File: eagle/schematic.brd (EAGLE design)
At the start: 40 x 40 mm, 23 parts, among them IC1 PIC18F1320SO, U1 MIC5205, U2 SG-3040LCLC

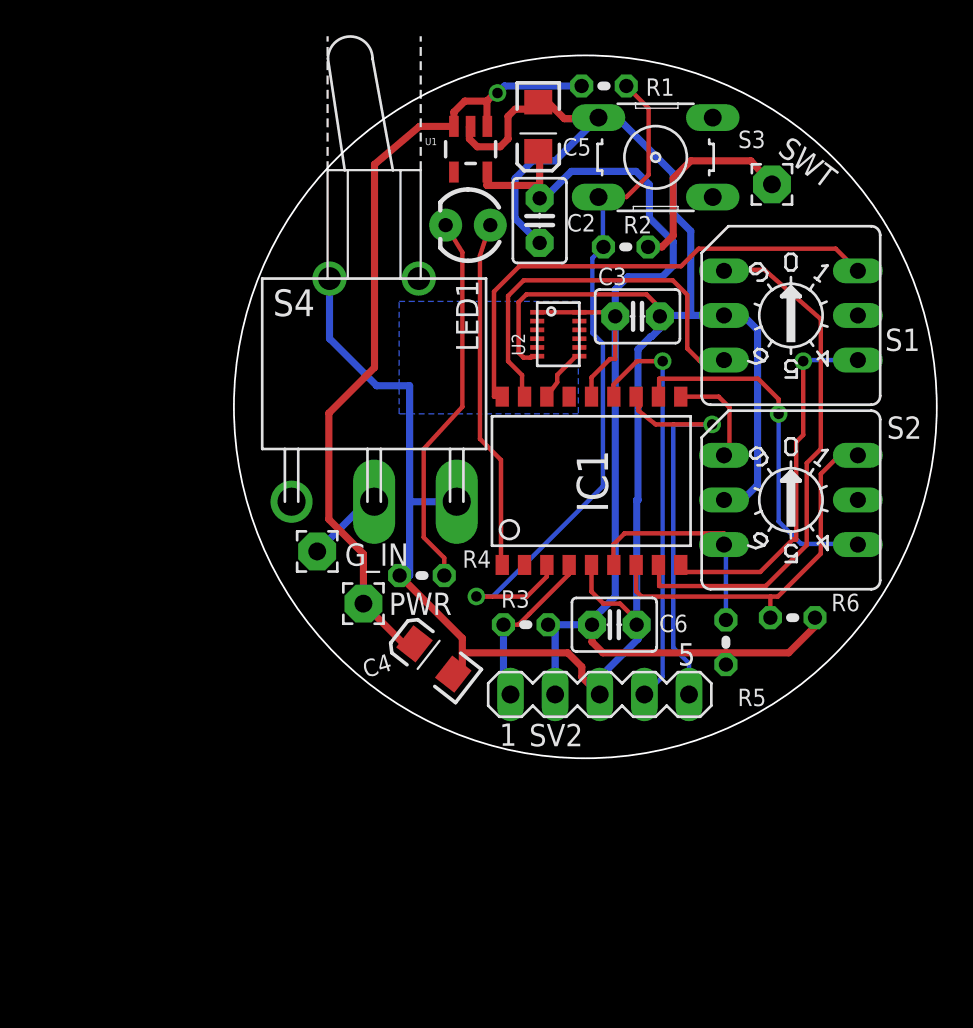
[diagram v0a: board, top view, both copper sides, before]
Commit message: Replaced ICD board header with a JST-EH connector
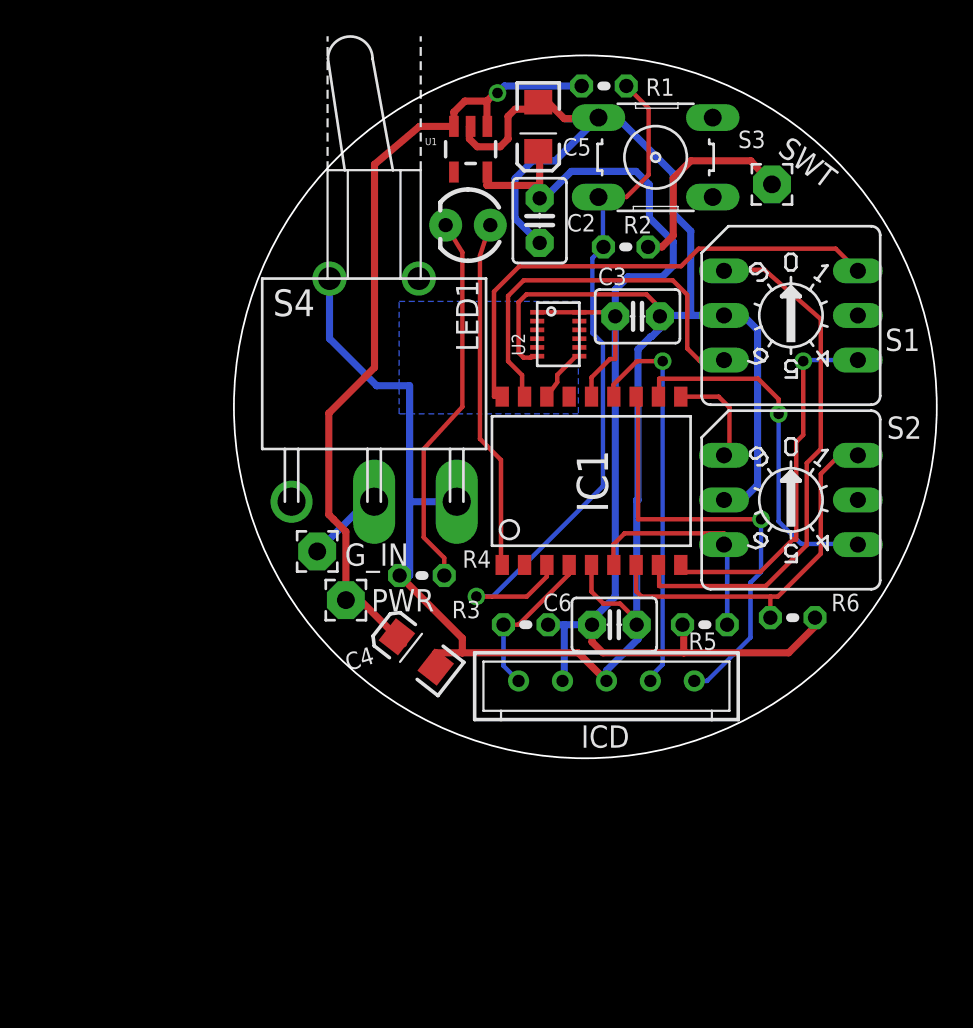
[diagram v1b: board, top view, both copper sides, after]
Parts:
- removed SV2: ICD, con-lstb:MA05-1
- added ICD: B4B-ZR, untitled:B5B-EH
- R5, R6: value 4.7K -> 10K
- moved R5 1.56 mm to (26.8, 7.60), turned to 180 degrees
- moved C4 1.08 mm to (10.4, 6.05)
- moved PWR 1.02 mm to (6.37, 9.00)
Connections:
- net GND: now also ICD.3; no longer SV2.3
- net N$6: now also ICD.1; no longer SV2.1
- net N$7: now also ICD.4; no longer SV2.4
- net N$8: now also ICD.5; no longer SV2.5
- net VDD: now also ICD.2; no longer SV2.2
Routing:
- net N$8: track 23.2 -> 25.3 mm
- net N$7: track 23.5 -> 22.5 mm
- net GND: track 136.8 -> 136.2 mm
- net N$6: track 9.98 -> 9.40 mm

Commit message: Added larger JC variant of oscillator to the underside of the PCB
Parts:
- added U$1: SG-3030,40(LC,JC,JF)JC, untitled:JC_TYPE
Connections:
- net CLK: now also U$1.3
- net GND: now also U$1.2
- net VDD: now also U$1.1, U$1.4
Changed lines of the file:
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@@
 <attribute name="NAME" x="19.75" y="0.6" size="1.27" layer="25"/>
 </element>
+<element name="U$1" library="untitled" package="JC_TYPE" value="SG-3030,40(LC,JC,JF)JC" x="-6" y="-10"/>
 </elements>
 <signals>
@@
 <wire x1="23" y1="6.785584375" x2="21.2" y2="4.985584375" width="0.4064" layer="16"/>
 <wire x1="21.2" y1="4.985584375" x2="21.2" y2="4.4" width="0.4064" layer="16"/>
+<contactref element="U$1" pad="2"/>
+<wire x1="-3.46" y1="-12.3" x2="11.4832125" y2="5.188071875" width="0" layer="19" extent="1-1"/>
 </signal>
 <signal name="CLK">
@@
 <wire x1="18.4" y1="21.81491875" x2="18.4" y2="21.4" width="0.254" layer="1"/>
 <wire x1="18.4" y1="21.4" x2="17.81" y2="20.5779" width="0.254" layer="1"/>
+<contactref element="U$1" pad="3"/>
+<wire x1="-3.46" y1="-7.7" x2="17.6032" y2="20.4622" width="0" layer="19" extent="1-1"/>
 </signal>
 <signal name="V+">
@@
 <wire x1="18.7" y1="4.4" x2="18.8" y2="4.4" width="0.4064" layer="16"/>
 <wire x1="18.8" y1="4.4" x2="18.8" y2="7.6" width="0.4064" layer="16"/>
+<contactref element="U$1" pad="1"/>
+<contactref element="U$1" pad="4"/>
+<wire x1="-8.54" y1="-7.7" x2="18.7" y2="4.4" width="0" layer="19" extent="1-1"/>
+<wire x1="-8.54" y1="-12.3" x2="-8.54" y2="-7.7" width="0" layer="19" extent="1-1"/>
 </signal>
 <signal name="N$1">

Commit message: Redo layout of extra oscillator
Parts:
- removed U$1: SG-3030,40(LC,JC,JF)JC, untitled:JC_TYPE
- added U3: SG-3030JC, untitled:JC_TYPE
- U2: value SG-3040LCLC -> SG-3040LC
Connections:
- net CLK: now also U3.3; no longer U$1.3
- net GND: now also U3.2; no longer U$1.2
- net VDD: now also U3.1, U3.4; no longer U$1.1, U$1.4
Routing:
- net VDD: track 74.9 -> 99.3 mm
- net CLK: track 3.36 -> 12.9 mm, vias 0 -> 1
- net GND: track 136.2 -> 141.7 mm
- removed copper zone on layer 16, net GND
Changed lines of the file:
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@@
 <attribute name="VALUE" x="2.718" y="35.18" size="1.524" layer="27" ratio="10" rot="R270"/>
 </element>
-<element name="U2" library="untitled" package="SOJ-12" value="SG-3040LCLC" x="18.46" y="24.13" smashed="yes" rot="R270">
+<element name="U2" library="untitled" package="SOJ-12" value="SG-3040LC" x="18.46" y="24.13" smashed="yes" rot="R270">
 <attribute name="NAME" x="16.187" y="23.5554" size="0.762" layer="25" font="vector" rot="R270" align="center"/>
 </element>
@@
 <attribute name="NAME" x="19.75" y="0.6" size="1.27" layer="25"/>
 </element>
-<element name="U$1" library="untitled" package="JC_TYPE" value="SG-3030,40(LC,JC,JF)JC" x="-6" y="-10"/>
+<element name="U3" library="untitled" package="JC_TYPE" value="SG-3030JC" x="14" y="22.4" smashed="yes" rot="MR180">
+<attribute name="NAME" x="5.41" y="19.66" size="1.27" layer="26" rot="MR90"/>
+<attribute name="VALUE" x="7.12" y="19.66" size="1.27" layer="28" rot="MR90"/>
+</element>
 </elements>
 <signals>
@@
 <wire x1="28.97538125" y1="25.2" x2="27.89" y2="25.2" width="0.4064" layer="16"/>
 <wire x1="10" y1="10.4" x2="10" y2="14.6" width="0.4064" layer="16"/>
-<wire x1="10" y1="14.6" x2="10" y2="21.2" width="0.4064" layer="16"/>
-<polygon width="0.254" layer="16" orphans="yes">
-<vertex x="9.4" y="26"/>
-<vertex x="19.6" y="26"/>
-<vertex x="19.6" y="19.6"/>
-<vertex x="9.4" y="19.6"/>
-</polygon>
+<wire x1="10" y1="14.6" x2="10" y2="17.478890625" width="0.4064" layer="16"/>
+<wire x1="10" y1="17.478890625" x2="9.278890625" y2="18.2" width="0.4064" layer="16"/>
+<wire x1="9.278890625" y1="18.2" x2="6.416521875" y2="18.2" width="0.4064" layer="16"/>
+<wire x1="6.416521875" y1="18.2" x2="5.44" y2="19.176521875" width="0.4064" layer="16"/>
+<wire x1="5.44" y1="19.176521875" x2="5.44" y2="27.3" width="0.4064" layer="16"/>
 <contactref element="S4" pad="3"/>
 <contactref element="S4" pad="B"/>
 <wire x1="13" y1="6" x2="19.6" y2="6" width="0.4064" layer="1"/>
 <wire x1="19.6" y1="6" x2="21.2" y2="4.4" width="0.4064" layer="1"/>
-<wire x1="10" y1="21.2" x2="8.1220875" y2="21.2" width="0.4064" layer="16"/>
-<wire x1="8.1220875" y1="21.2" x2="5.44" y2="23.8820875" width="0.4064" layer="16"/>
-<wire x1="5.44" y1="23.8820875" x2="5.44" y2="27.3" width="0.4064" layer="16"/>
 <wire x1="10" y1="10.4" x2="9.43" y2="10.4" width="0.4064" layer="16"/>
 <wire x1="12.68" y1="14.6" x2="10" y2="14.6" width="0.4064" layer="16"/>
@@
 <wire x1="23" y1="6.785584375" x2="21.2" y2="4.985584375" width="0.4064" layer="16"/>
 <wire x1="21.2" y1="4.985584375" x2="21.2" y2="4.4" width="0.4064" layer="16"/>
-<contactref element="U$1" pad="2"/>
-<wire x1="-3.46" y1="-12.3" x2="11.4832125" y2="5.188071875" width="0" layer="19" extent="1-1"/>
+<contactref element="U3" pad="2"/>
+<wire x1="16.54" y1="24.7" x2="16.54" y2="28.47" width="0.4064" layer="16"/>
+<wire x1="16.54" y1="28.47" x2="17.4" y2="29.33" width="0.4064" layer="16"/>
 </signal>
 <signal name="CLK">
@@
 <wire x1="18.4" y1="21.81491875" x2="18.4" y2="21.4" width="0.254" layer="1"/>
 <wire x1="18.4" y1="21.4" x2="17.81" y2="20.5779" width="0.254" layer="1"/>
-<contactref element="U$1" pad="3"/>
-<wire x1="-3.46" y1="-7.7" x2="17.6032" y2="20.4622" width="0" layer="19" extent="1-1"/>
+<contactref element="U3" pad="3"/>
+<wire x1="17.6032" y1="20.4622" x2="18" y2="20.4622" width="0.254" layer="1"/>
+<wire x1="18" y1="20.4622" x2="18" y2="16" width="0.254" layer="1"/>
+<wire x1="18" y1="16" x2="16.54" y2="17.46" width="0.254" layer="16"/>
+<wire x1="16.54" y1="17.46" x2="16.54" y2="20.1" width="0.254" layer="16"/>
+<via x="18" y="16" extent="1-16" drill="0.6" shape="square"/>
 </signal>
 <signal name="V+">
@@
 <wire x1="18.7" y1="4.4" x2="18.8" y2="4.4" width="0.4064" layer="16"/>
 <wire x1="18.8" y1="4.4" x2="18.8" y2="7.6" width="0.4064" layer="16"/>
-<contactref element="U$1" pad="1"/>
-<contactref element="U$1" pad="4"/>
-<wire x1="-8.54" y1="-7.7" x2="18.7" y2="4.4" width="0" layer="19" extent="1-1"/>
-<wire x1="-8.54" y1="-12.3" x2="-8.54" y2="-7.7" width="0" layer="19" extent="1-1"/>
+<contactref element="U3" pad="1"/>
+<contactref element="U3" pad="4"/>
+<wire x1="11.46" y1="20.1" x2="11.46" y2="24.7" width="0.4064" layer="16"/>
+<wire x1="11.46" y1="24.7" x2="11.46" y2="22.6" width="0.4064" layer="16"/>
+<wire x1="11.46" y1="22.6" x2="19.2" y2="22.6" width="0.4064" layer="16"/>
+<wire x1="19.2" y1="22.6" x2="19.2" y2="30.07" width="0.4064" layer="16"/>
+<wire x1="19.2" y1="30.07" x2="17.4" y2="31.87" width="0.4064" layer="16"/>
 </signal>
 <signal name="N$1">

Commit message: Files missing from the previous commit
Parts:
- C3: value 0.1 uF -> 0.22uF
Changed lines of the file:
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@@
 <attribute name="VALUE" x="15.752" y="27.051" size="0.9906" layer="27" ratio="10"/>
 </element>
-<element name="C3" library="capacitor-wima" package="C2.5-3" value="0.1 uF" x="22.97" y="25.15" smashed="yes">
-<attribute name="NAME" x="20.719" y="26.928" size="0.9906" layer="25" ratio="10"/>
-<attribute name="VALUE" x="20.319" y="22.302" size="0.9906" layer="27" ratio="10"/>
+<element name="C3" library="capacitor-wima" package="C2.5-3" value="0.22uF" x="22.97" y="25.15" smashed="yes">
+<attribute name="NAME" x="20.519" y="22.328" size="0.9906" layer="25" ratio="10"/>
+<attribute name="VALUE" x="20.719" y="26.902" size="0.9906" layer="27" ratio="10"/>
 </element>
 <element name="C4" library="SparkFun" package="EIA3216" value="10uF" x="10.38" y="6.05" smashed="yes" rot="R142">

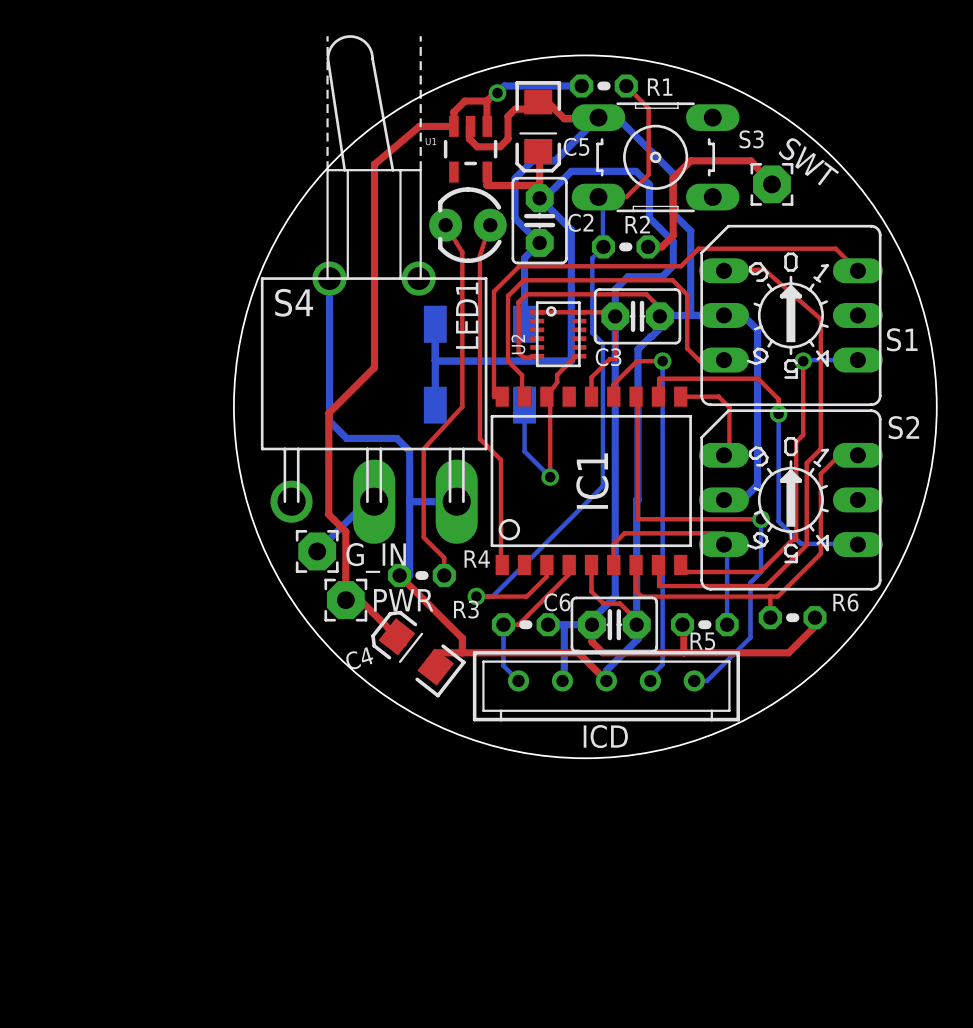
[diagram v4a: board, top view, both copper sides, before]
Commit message: Correct wiring of manual push switch, larger holes for ICD, increase U2 footprint
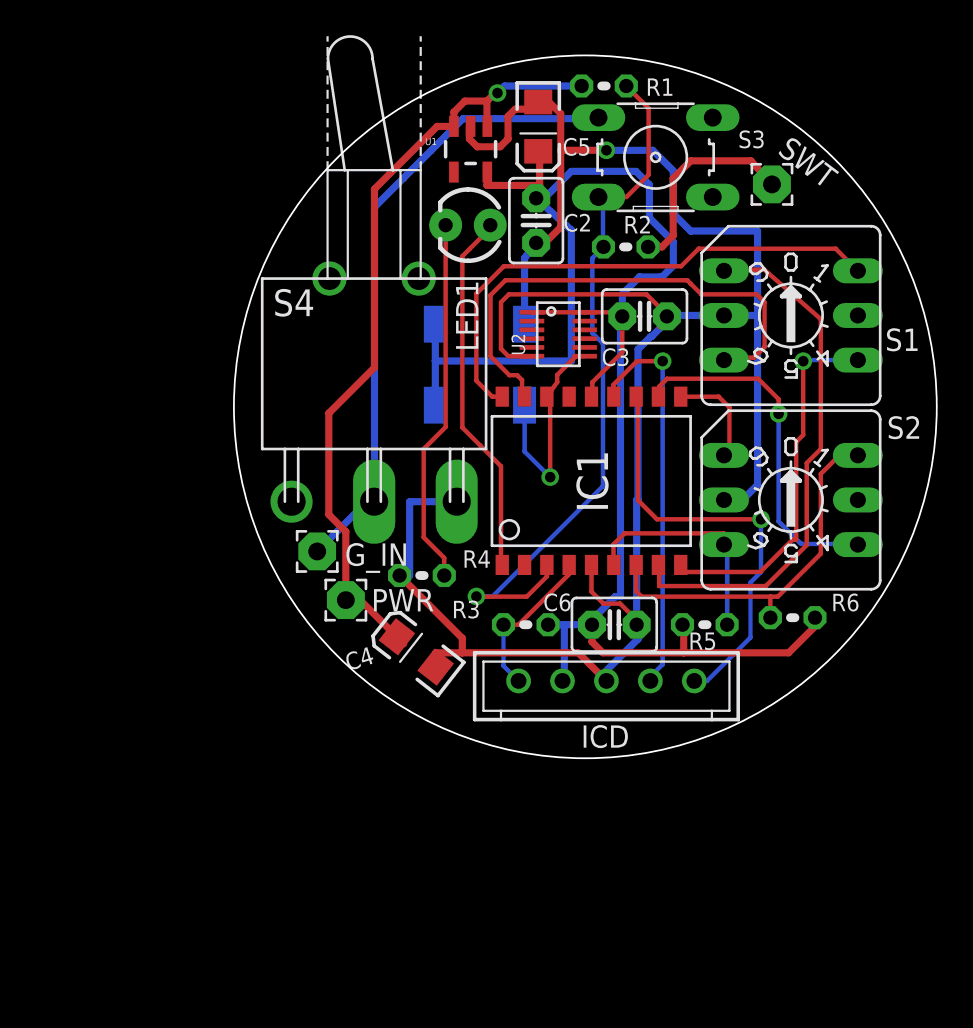
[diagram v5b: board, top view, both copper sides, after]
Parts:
- U2: device untitled:SOJ-12 -> untitled:SOJ-12-L
- moved C3 0.40 mm to (23.4, 25.1)
- moved C2 0.20 mm to (17.2, 30.6)
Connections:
- removed net GND: C2.2, C3.2, C4.C, C5.C, C6.2, IC1.5, ICD.3, R4.2, S1.C, S2.C, S3.4, S4.3, S4.B, U1.2, U2.6, U3.2
- removed net SWITCHED_GND: G_IN.1, S4.2
- new net GND1: G_IN.1, S3.4, S4.2
- new net N$12: C2.2, C3.2, C4.C, C5.C, C6.2, IC1.5, ICD.3, R4.2, S1.C, S2.C, S4.3, U1.2, U2.6, U3.2
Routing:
- net GND: track 141.7 -> 0.00 mm
- net N$12: track 0.00 -> 127.2 mm, vias 0 -> 1
- net GND1: track 0.00 -> 36.1 mm
- net SWITCH_OUT_2: track 22.6 -> 28.6 mm
- net SWITCHED_GND: track 4.41 -> 0.00 mm
- net SWITCH_OUT_3: track 28.7 -> 30.1 mm
- net VDD: track 99.3 -> 97.9 mm
- net N$10: track 20.1 -> 21.0 mm
- net V+: track 46.1 -> 45.4 mm
- net N$8: track 25.3 -> 24.7 mm
- net N$11: track 21.5 -> 20.9 mm

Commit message: Create new set of gerber files
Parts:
- R4: value 1K -> 523R
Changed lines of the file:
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@@
 <attribute name="VALUE" x="11.4764" y="6.6886" size="0.9906" layer="27" ratio="10"/>
 </element>
-<element name="R4" library="resistor" package="0204V" value="1K" x="10.7" y="10.4" smashed="yes" rot="R180">
+<element name="R4" library="resistor" package="0204V" value=" 523R" x="10.7" y="10.4" smashed="yes" rot="R180">
 <attribute name="NAME" x="14.6336" y="11.8316" size="0.9906" layer="25" ratio="10" rot="R180"/>
 <attribute name="VALUE" x="14.4336" y="10.7114" size="0.9906" layer="27" ratio="10" rot="R180"/>
